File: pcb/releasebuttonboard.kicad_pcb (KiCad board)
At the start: 2 copper layers, 65 x 56 mm, 30 parts, among them SW1 ROTENC, U1 24C16, U2 RASPIPLUSHEADER, U3 OLEDHeader, U4 REncHeader, U5 BtnHeader, U6 PAM8407, U7 REncHeader

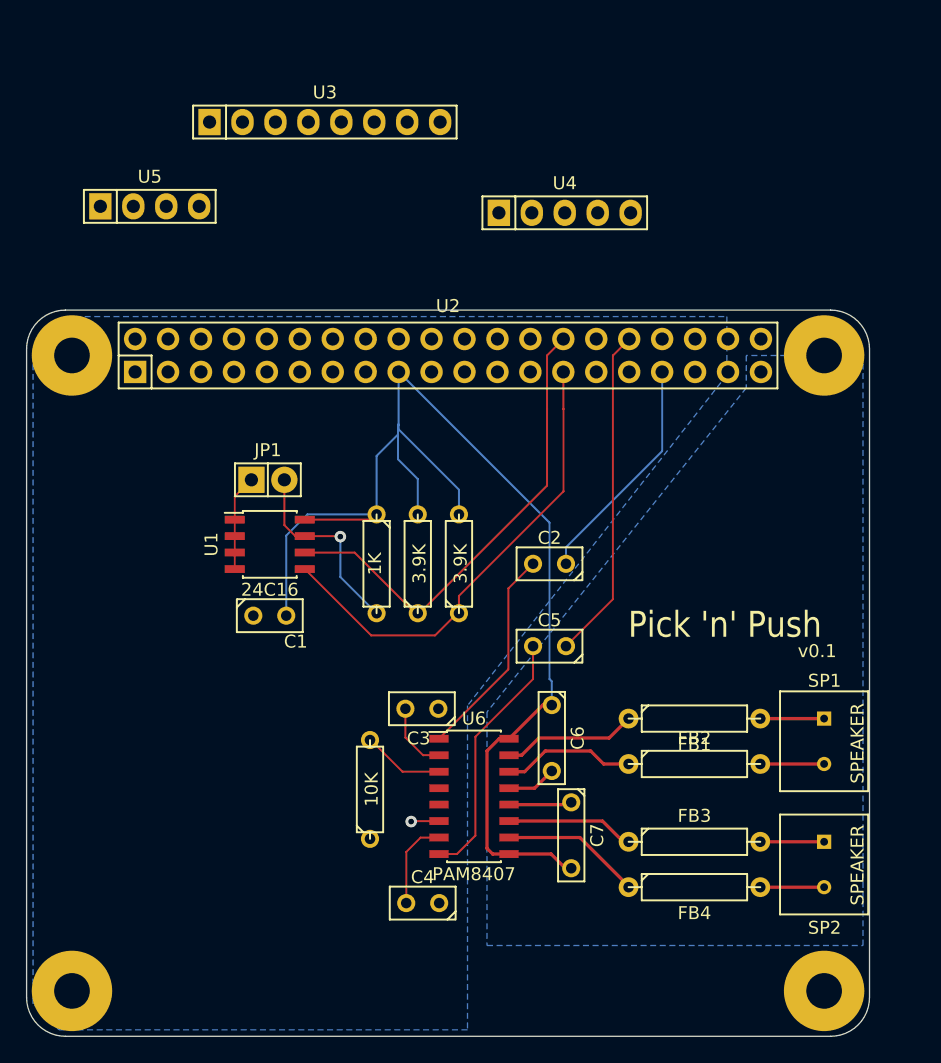
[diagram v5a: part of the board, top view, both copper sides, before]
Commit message: Update PCB for new netlist.
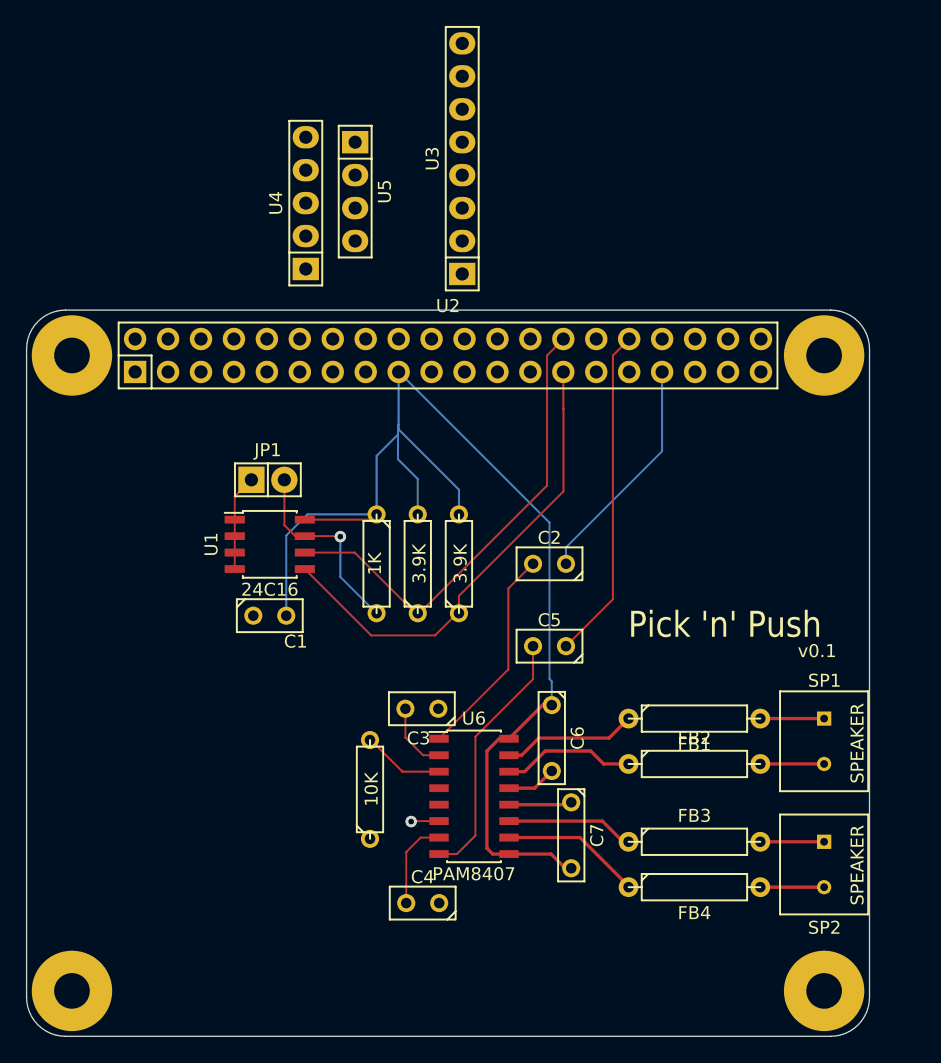
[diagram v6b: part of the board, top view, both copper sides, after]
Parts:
- moved U4 20.0 mm to (117.0, 59.8), turned to 90 degrees
- moved U5 15.9 mm to (120.8, 58.9), turned to 270 degrees
- moved U3 11.0 mm to (129.1, 56.3), turned to 90 degrees
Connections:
- U2 pad 10: /OLEDDC -> (no net)
- U2 pad 11: /BTNLED -> /MNUROTA
- U2 pad 12: /BTNPUSH -> /MNUROTB
- U2 pad 15: Net-(U2-Pad15) -> /BTNLED
- U2 pad 16: Net-(U2-Pad16) -> /BTNPUSH
- U2 pad 18: Net-(U2-Pad18) -> /OLEDRST
- U2 pad 2: Net-(U2-Pad2) -> (no net)
- U2 pad 21: Net-(U2-Pad21) -> (no net)
- U2 pad 22: /MNUROTA -> /OLEDDC
- U2 pad 26: Net-(U2-Pad26) -> (no net)
- U2 pad 29: Net-(U2-Pad29) -> (no net)
- U2 pad 3: Net-(U2-Pad3) -> (no net)
- U2 pad 31: Net-(U2-Pad31) -> (no net)
- U2 pad 35: Net-(U2-Pad35) -> (no net)
- U2 pad 36: Net-(U2-Pad36) -> (no net)
- U2 pad 37: /MNUROTB -> (no net)
- U2 pad 38: Net-(U2-Pad38) -> (no net)
- U2 pad 4: Net-(U2-Pad4) -> (no net)
- U2 pad 40: Net-(U2-Pad40) -> (no net)
- U2 pad 5: Net-(U2-Pad5) -> (no net)
- U2 pad 7: Net-(U2-Pad7) -> (no net)
- U2 pad 8: /OLEDRST -> (no net)
- U3 pad 6: Net-(U3-Pad6) -> (no net)
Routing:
- removed copper zone on B.Cu, net GND

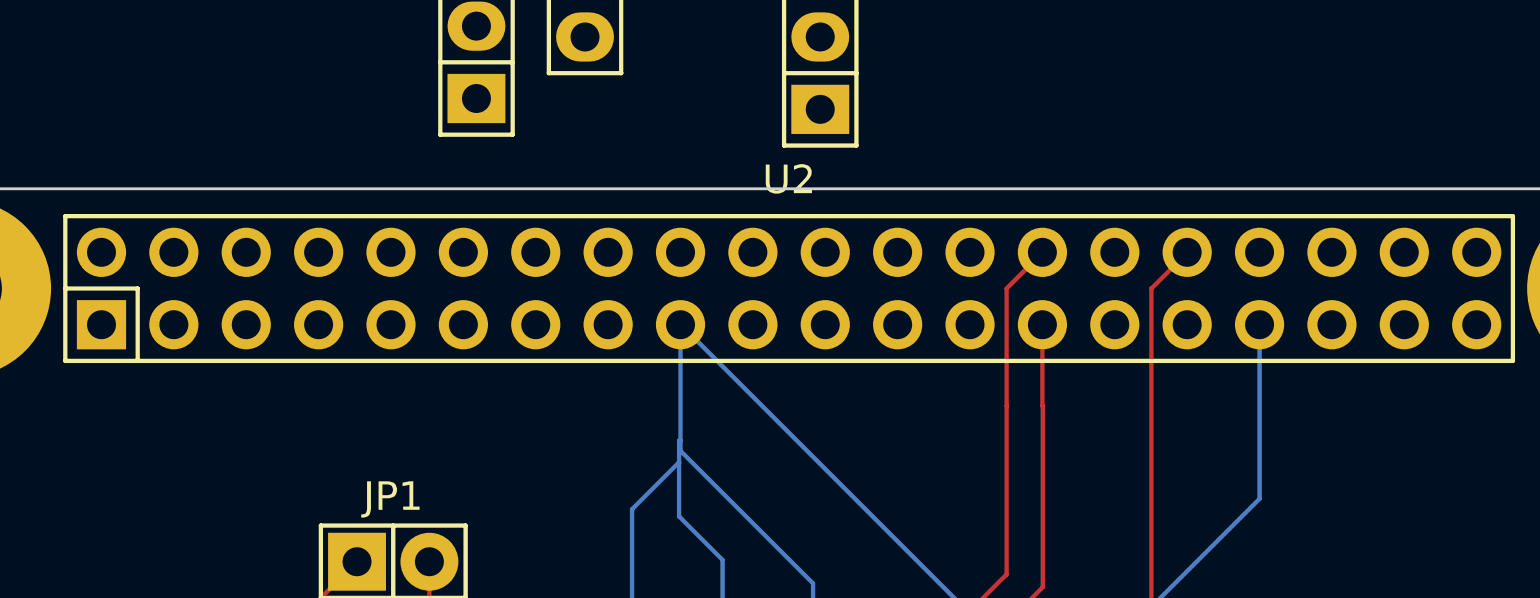
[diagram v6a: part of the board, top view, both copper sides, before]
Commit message: Power the audio amp from the 5V supply.
This should keep it a little more isolated from the digital supply as well
as making it easier to route the power tracks.
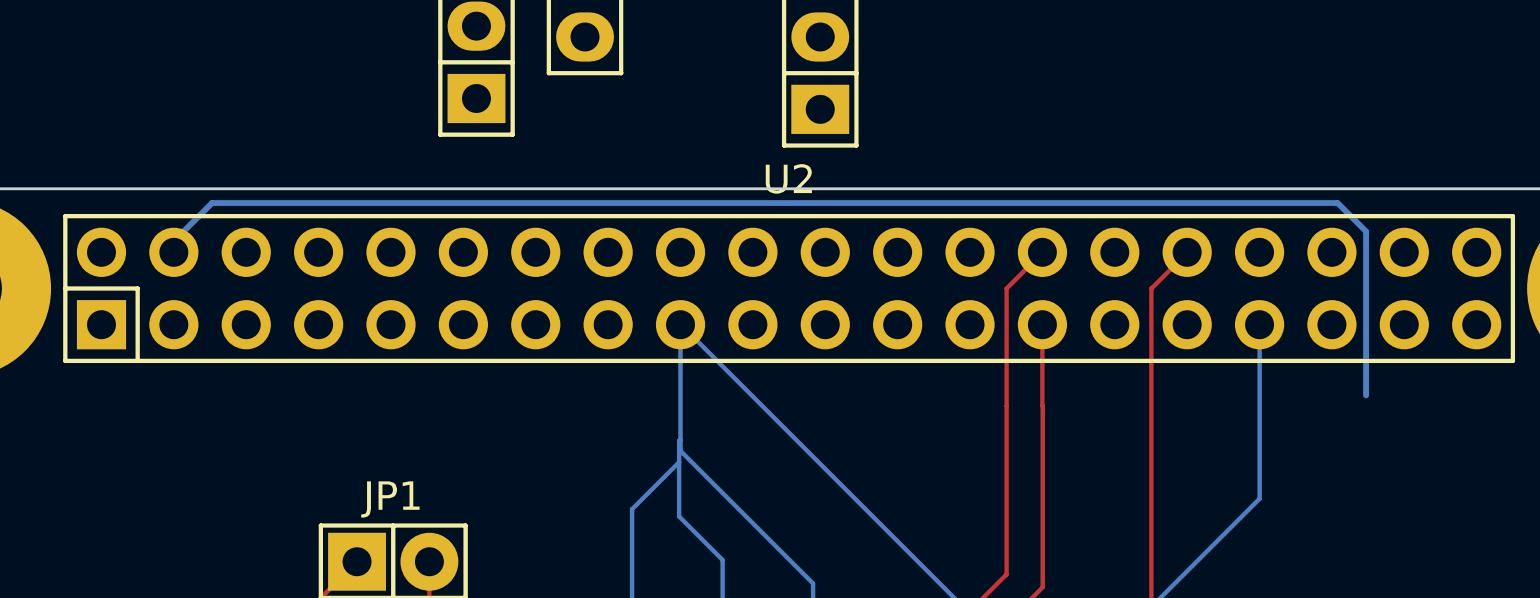
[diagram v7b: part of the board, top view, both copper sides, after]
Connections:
- C6 pad 1: VCC -> AVCC
- C7 pad 2: VCC -> AVCC
- U2 pad 2: (no net) -> AVCC
- U2 pad 4: (no net) -> AVCC
- U6 pad 16: VCC -> AVCC
- U6 pad 9: VCC -> AVCC
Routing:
- net AVCC: track 0.00 -> 71.9 mm
- net VCC: track 99.1 -> 76.1 mm
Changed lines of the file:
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@@
 (kicad_pcb (version 4) (host pcbnew "(2014-jul-16 BZR unknown)-product")
   (general
-    (links 75)
-    (no_connects 39)
+    (links 76)
+    (no_connects 41)
     (area 95.449999 67.949999 160.550001 124.050001)
     (thickness 1.6)
     (drawings 10)
-    (tracks 115)
+    (tracks 120)
     (zones 0)
     (modules 30)
-    (nets 36)
+    (nets 37)
   )
   (page A4)
@@
   )
   (setup
-    (last_trace_width 0.1524)
+    (last_trace_width 0.2032)
     (user_trace_width 0.2032)
     (trace_clearance 0.1524)
@@
   (net 34 /OLEDCS)
   (net 35 /MNUROTB)
+  (net 36 AVCC)
   (net_class Default "This is the default net class."
     (clearance 0.1524)
@@
     (add_net /OLEDDC)
     (add_net /OLEDRST)
+    (add_net AVCC)
     (add_net GND)
     (add_net "Net-(C2-Pad2)")
@@
     (fp_line (start -3.556 -0.508) (end -3.048 -1.016) (layer F.SilkS) (width 0.15))
     (pad 1 thru_hole circle (at -2.54 0 270) (size 1.397 1.397) (drill 0.8128) (layers *.Cu *.Mask F.SilkS)
-      (net 2 VCC))
+      (net 36 AVCC))
     (pad 2 thru_hole circle (at 2.54 0 270) (size 1.397 1.397) (drill 0.8128) (layers *.Cu *.Mask F.SilkS)
       (net 1 GND))
@@
       (net 1 GND))
     (pad 2 thru_hole circle (at 2.54 0 270) (size 1.397 1.397) (drill 0.8128) (layers *.Cu *.Mask F.SilkS)
-      (net 2 VCC))
+      (net 36 AVCC))
     (model Discret/C2.wrl
       (at (xyz 0 0 0))
@@
     (pad 1 thru_hole rect (at -24.13 1.27) (size 1.7272 1.7272) (drill 1.016) (layers *.Cu *.Mask F.SilkS)
       (net 2 VCC))
-    (pad 2 thru_hole oval (at -24.13 -1.27) (size 1.7272 1.7272) (drill 1.016) (layers *.Cu *.Mask F.SilkS))
+    (pad 2 thru_hole oval (at -24.13 -1.27) (size 1.7272 1.7272) (drill 1.016) (layers *.Cu *.Mask F.SilkS)
+      (net 36 AVCC))
     (pad 3 thru_hole oval (at -21.59 1.27) (size 1.7272 1.7272) (drill 1.016) (layers *.Cu *.Mask F.SilkS))
-    (pad 4 thru_hole oval (at -21.59 -1.27) (size 1.7272 1.7272) (drill 1.016) (layers *.Cu *.Mask F.SilkS))
+    (pad 4 thru_hole oval (at -21.59 -1.27) (size 1.7272 1.7272) (drill 1.016) (layers *.Cu *.Mask F.SilkS)
+      (net 36 AVCC))
     (pad 5 thru_hole oval (at -19.05 1.27) (size 1.7272 1.7272) (drill 1.016) (layers *.Cu *.Mask F.SilkS))
     (pad 6 thru_hole oval (at -19.05 -1.27) (size 1.7272 1.7272) (drill 1.016) (layers *.Cu *.Mask F.SilkS)
@@
       (net 8 "Net-(C5-Pad2)"))
     (pad 9 smd rect (at 2.7 4.445) (size 1.5 0.6) (layers F.Cu F.Paste F.Mask)
-      (net 2 VCC))
+      (net 36 AVCC))
     (pad 10 smd rect (at 2.7 3.175) (size 1.5 0.6) (layers F.Cu F.Paste F.Mask)
       (net 15 "Net-(FB4-Pad1)"))
@@
       (net 9 "Net-(FB1-Pad1)"))
     (pad 16 smd rect (at 2.7 -4.445) (size 1.5 0.6) (layers F.Cu F.Paste F.Mask)
-      (net 2 VCC))
+      (net 36 AVCC))
     (model Housings_SOIC/SOIC-16_3.9x9.9mm_Pitch1.27mm.wrl
       (at (xyz 0 0 0))
@@
   (segment (start 135.825 84.39) (end 135.825 96.455) (width 0.1524) (layer B.Cu) (net 2))
   (segment (start 124.205 72.77) (end 135.825 84.39) (width 0.1524) (layer B.Cu) (net 2))
-  (segment (start 136 96.63) (end 136 98.46) (width 0.1524) (layer B.Cu) (net 2))
   (segment (start 135.825 96.455) (end 136 96.63) (width 0.1524) (layer B.Cu) (net 2))
   (segment (start 124.19 72.77) (end 124.205 72.77) (width 0.1524) (layer B.Cu) (net 2))
   (segment (start 124.19 72.77) (end 124.19 73.19) (width 0.254) (layer F.Cu) (net 2))
   (segment (start 124.19 72.77) (end 124.27 72.77) (width 0.254) (layer F.Cu) (net 2))
-  (segment (start 132.7 101.055) (end 131.945 101.055) (width 0.254) (layer F.Cu) (net 2))
-  (segment (start 131.445 109.945) (end 132.7 109.945) (width 0.254) (layer F.Cu) (net 2))
-  (segment (start 131 109.5) (end 131.445 109.945) (width 0.254) (layer F.Cu) (net 2))
-  (segment (start 131 102) (end 131 109.5) (width 0.254) (layer F.Cu) (net 2))
-  (segment (start 131.945 101.055) (end 131 102) (width 0.254) (layer F.Cu) (net 2))
-  (segment (start 136 98.46) (end 135.295 98.46) (width 0.254) (layer F.Cu) (net 2))
-  (segment (start 135.295 98.46) (end 132.7 101.055) (width 0.254) (layer F.Cu) (net 2))
-  (segment (start 137.5 111.04) (end 137.04 111.04) (width 0.254) (layer F.Cu) (net 2))
-  (segment (start 137.04 111.04) (end 135.945 109.945) (width 0.254) (layer F.Cu) (net 2))
-  (segment (start 135.945 109.945) (end 132.7 109.945) (width 0.254) (layer F.Cu) (net 2))
   (segment (start 137.095 87.565) (end 137.095 86.295) (width 0.1524) (layer B.Cu) (net 3))
   (segment (start 144.51 78.88) (end 144.51 72.77) (width 0.1524) (layer B.Cu) (net 3))
@@
   (segment (start 122.0455 101.154) (end 124.4865 103.595) (width 0.1524) (layer F.Cu) (net 20))
   (segment (start 124.4865 103.595) (end 127.3 103.595) (width 0.1524) (layer F.Cu) (net 20))
+  (segment (start 106.41 70.23) (end 106.41 69.84) (width 0.2032) (layer B.Cu) (net 36) (status C00000))
+  (segment (start 106.41 69.84) (end 107.75 68.5) (width 0.2032) (layer B.Cu) (net 36) (status 400000))
+  (segment (start 107.75 68.5) (end 147.25 68.5) (width 0.2032) (layer B.Cu) (net 36))
+  (segment (start 147.25 68.5) (end 148.25 69.5) (width 0.2032) (layer B.Cu) (net 36))
+  (segment (start 148.25 69.5) (end 148.25 75.25) (width 0.2032) (layer B.Cu) (net 36))
+  (segment (start 136 96.63) (end 136 98.46) (width 0.1524) (layer B.Cu) (net 36))
+  (segment (start 132.7 101.055) (end 131.945 101.055) (width 0.254) (layer F.Cu) (net 36))
+  (segment (start 131.445 109.945) (end 132.7 109.945) (width 0.254) (layer F.Cu) (net 36))
+  (segment (start 131 109.5) (end 131.445 109.945) (width 0.254) (layer F.Cu) (net 36))
+  (segment (start 131 102) (end 131 109.5) (width 0.254) (layer F.Cu) (net 36))
+  (segment (start 131.945 101.055) (end 131 102) (width 0.254) (layer F.Cu) (net 36))
+  (segment (start 136 98.46) (end 135.295 98.46) (width 0.254) (layer F.Cu) (net 36))
+  (segment (start 135.295 98.46) (end 132.7 101.055) (width 0.254) (layer F.Cu) (net 36))
+  (segment (start 137.5 111.04) (end 137.04 111.04) (width 0.254) (layer F.Cu) (net 36))
+  (segment (start 137.04 111.04) (end 135.945 109.945) (width 0.254) (layer F.Cu) (net 36))
+  (segment (start 135.945 109.945) (end 132.7 109.945) (width 0.254) (layer F.Cu) (net 36))
 )

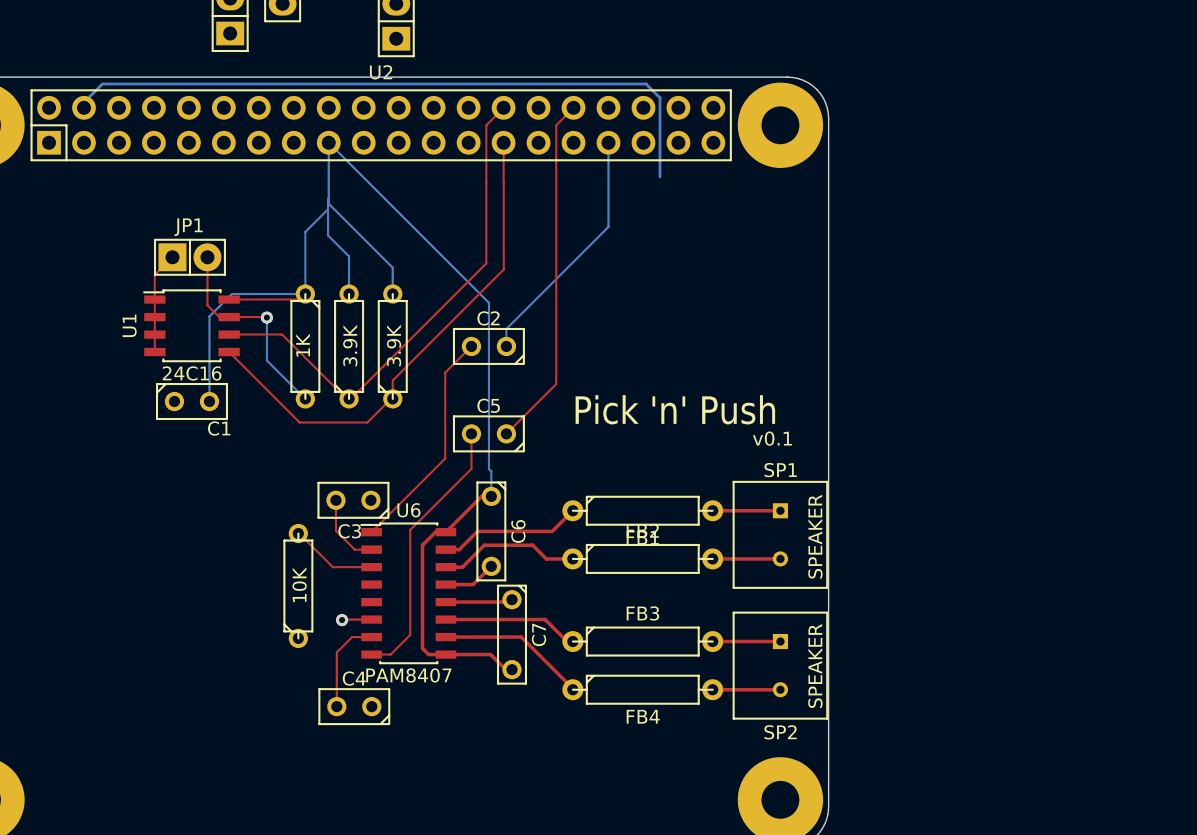
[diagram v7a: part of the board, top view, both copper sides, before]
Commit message: New vertical layout of the audio circuit.
Easier to fit everything in this way and provide clear ground return paths,
I hope. (Remains to be seen whether the traces will work out.)
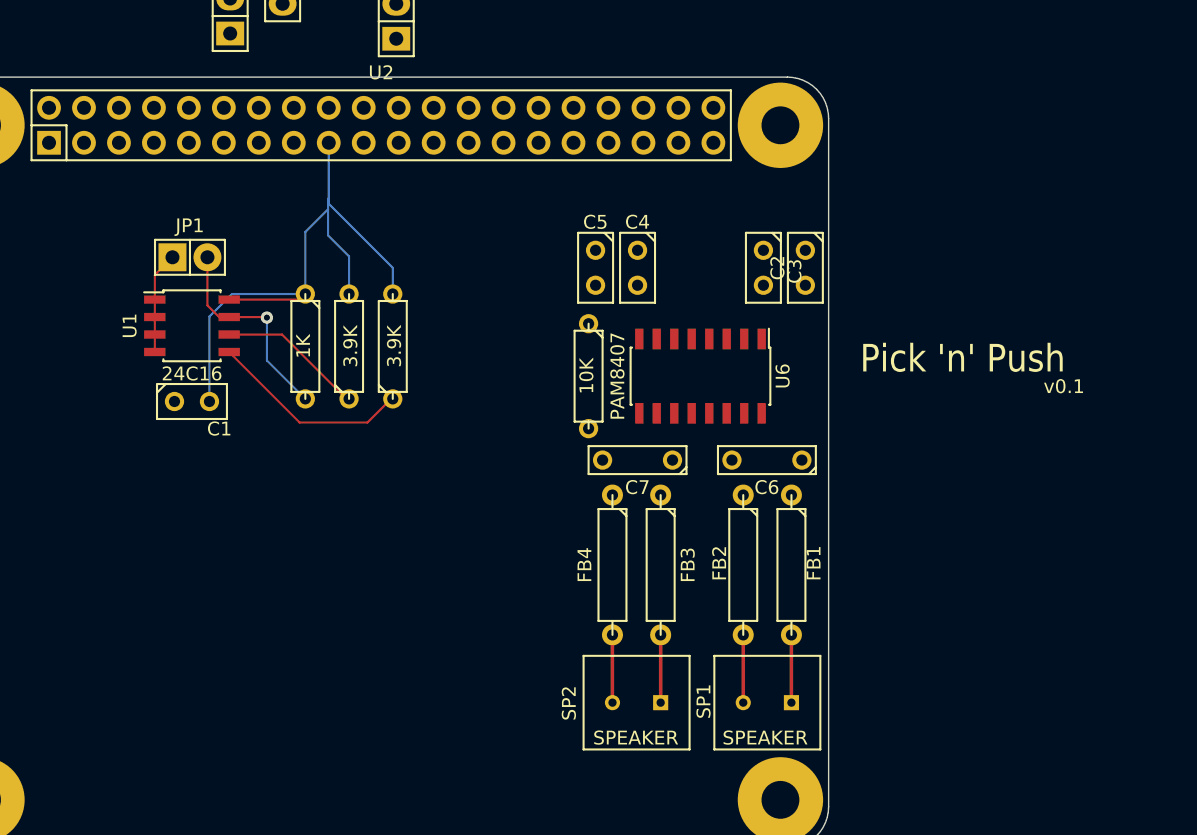
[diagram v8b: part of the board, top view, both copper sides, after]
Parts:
- moved C4 37.9 mm to (146.6, 81.8), turned to 270 degrees
- moved C3 34.2 mm to (155.8, 81.8), turned to 270 degrees
- moved U6 26.4 mm to (151.2, 89.7), turned to 270 degrees
- moved R4 26.0 mm to (143.1, 89.7), turned to 270 degrees
- moved C2 23.7 mm to (158.8, 81.8), turned to 270 degrees
- moved C6 20.7 mm to (156.0, 95.8), turned to 180 degrees
- moved C7 15.6 mm to (146.6, 95.8), turned to 180 degrees
- moved C5 14.3 mm to (143.6, 81.8), turned to 270 degrees
- moved SP1 14.0 mm to (157.8, 113.4), turned to 180 degrees
- moved FB1 11.5 mm to (157.8, 103.4), turned to 270 degrees
- moved SP2 9.77 mm to (148.3, 113.4), turned to 180 degrees
- moved FB4 9.32 mm to (144.8, 103.4), turned to 270 degrees
- moved FB2 7.31 mm to (154.3, 103.4), turned to 270 degrees
- moved FB3 5.71 mm to (148.3, 103.4), turned to 270 degrees
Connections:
- R4 pad 1: VCC -> AVCC
- U6 pad 4: VCC -> AVCC
- U6 pad 5: VCC -> AVCC
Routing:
- net AVCC: track 71.9 -> 0.39 mm
- net VCC: track 76.1 -> 47.4 mm
- net /ID_SC: track 36.5 -> 10.8 mm
- net /AUD_L: track 25.7 -> 0.01 mm
- net /ID_SD: track 36.7 -> 14.7 mm
- net Net-(C5-Pad2): track 19.8 -> 0.00 mm
- net /AUD_R: track 17.9 -> 0.00 mm
- net Net-(C2-Pad2): track 16.5 -> 0.00 mm
- net GND: track 18.3 -> 7.41 mm, vias 1 -> 0
- net Net-(FB4-Pad1): track 10.9 -> 0.08 mm
- net Net-(FB1-Pad1): track 10.4 -> 0.00 mm
- net Net-(FB2-Pad1): track 10.3 -> 0.00 mm
- net Net-(FB3-Pad1): track 10.6 -> 0.42 mm
- net Net-(C4-Pad2): track 6.92 -> 0.00 mm
- net Net-(R4-Pad2): track 6.33 -> 0.00 mm
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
